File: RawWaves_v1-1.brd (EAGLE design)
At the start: 107 x 20 mm, 56 parts, among them IC1 LM1117MP-5.0, IC4 TL074, U1 TEENSY_3.1_TW, U2 MIC803-26D4VM3TR, X1 VERT_SD_CARD_REV2

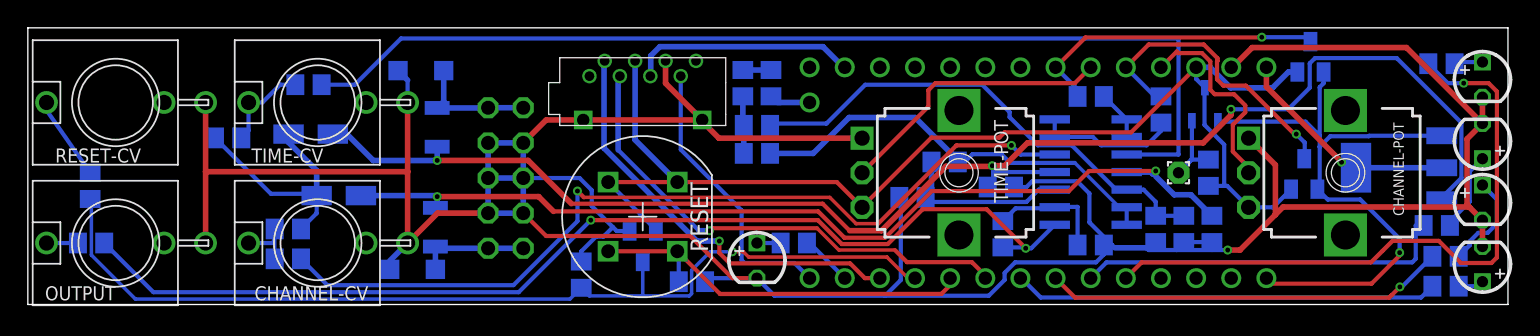
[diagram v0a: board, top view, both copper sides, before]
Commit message: Widen Pogo Hole
Replaced "Pogo 1.6/0.8" with "Pogo 1.6/0.9"
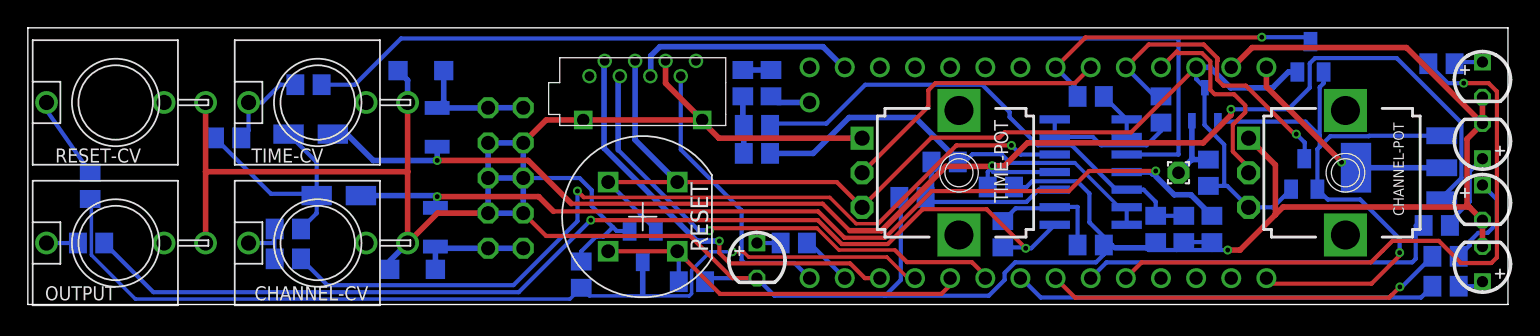
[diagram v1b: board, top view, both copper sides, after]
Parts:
- removed POGO: (no value), wirepad:1,6/0,8
- added PAD1: (no value), wirepad:1,6/0,9
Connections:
- net N$17: now also PAD1.1; no longer POGO.1
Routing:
- net N$17: track 6.72 -> 5.36 mm
- net -12V: track 70.5 -> 69.5 mm
- net N$13: track 8.14 -> 7.13 mm
- net N$11: track 6.65 -> 5.80 mm
- net GND: track 271.2 -> 270.4 mm
- net DGND: track 45.6 -> 44.9 mm
- net RESET_CV: track 71.8 -> 71.1 mm
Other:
- board text added: "Raw Waves v1.1 by Sherpa Modular, licensed under CC-BY-SA 3.0 This is a derivative work from "Radio Music" by Tom Whitwell, Which has been used under CC-BY-SA 3.0 www.sherpamodular.com"
- board text removed: "Raw Waves v1.0 by Sherpa Modular, licensed under CC-BY-SA 3.0 This is a derivative work from "Radio Music" by Tom Whitwell, Which has been used under CC-BY-SA 3.0 www.sherpamodular.com"
